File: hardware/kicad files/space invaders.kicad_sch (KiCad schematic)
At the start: 43 parts, among them J1 ICSP, J10 DE9_Socket, J2 RE, J3 RD, J4 RC5/6/7, J5 RC0/1/2, J6 RA6/7, J7 Conn_01x04_Pin, J8 RB1/2/3/4/5, J9 USB_C_Receptacle_PowerOnly_6P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

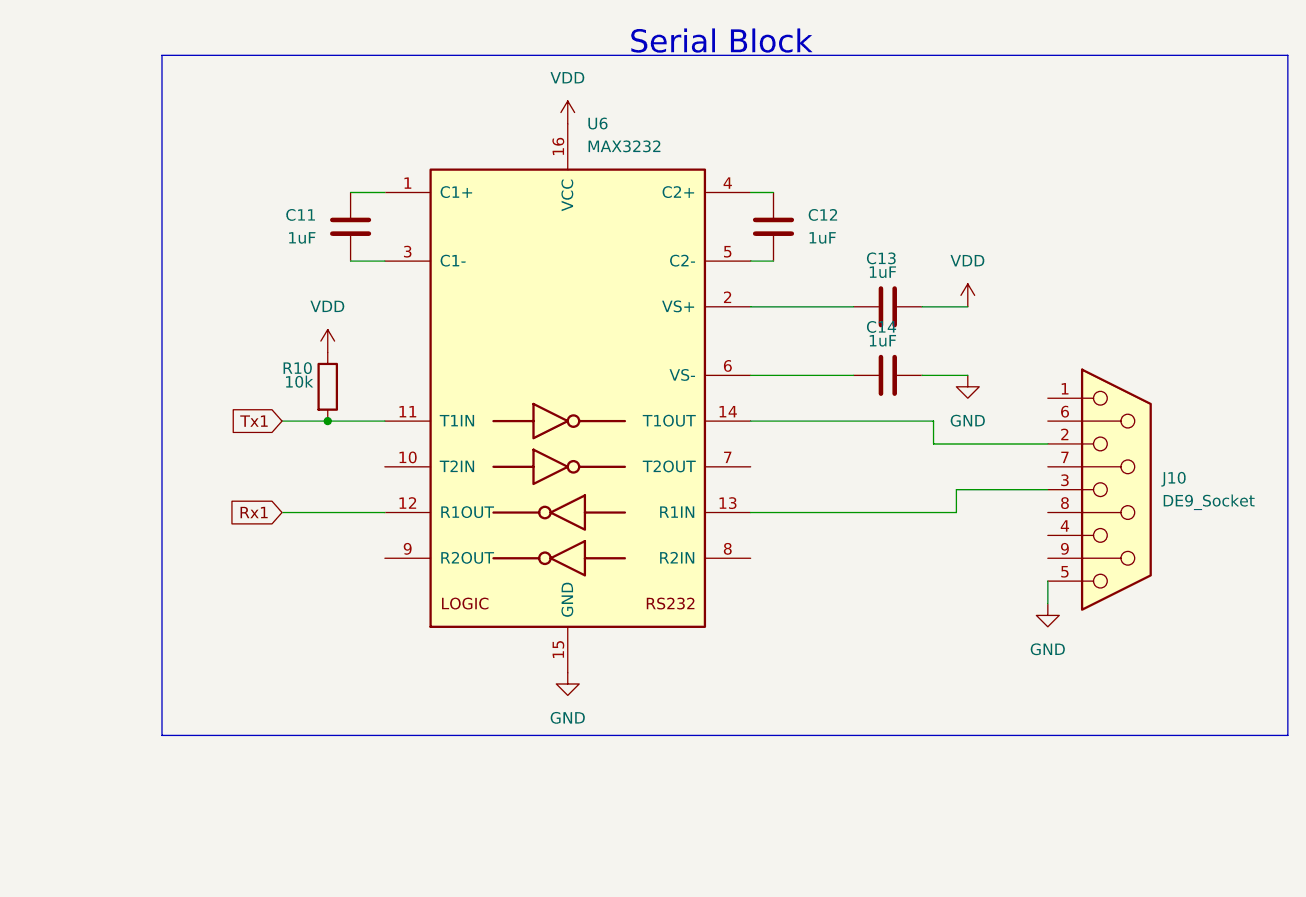
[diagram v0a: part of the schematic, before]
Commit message: Added Serial to PCB
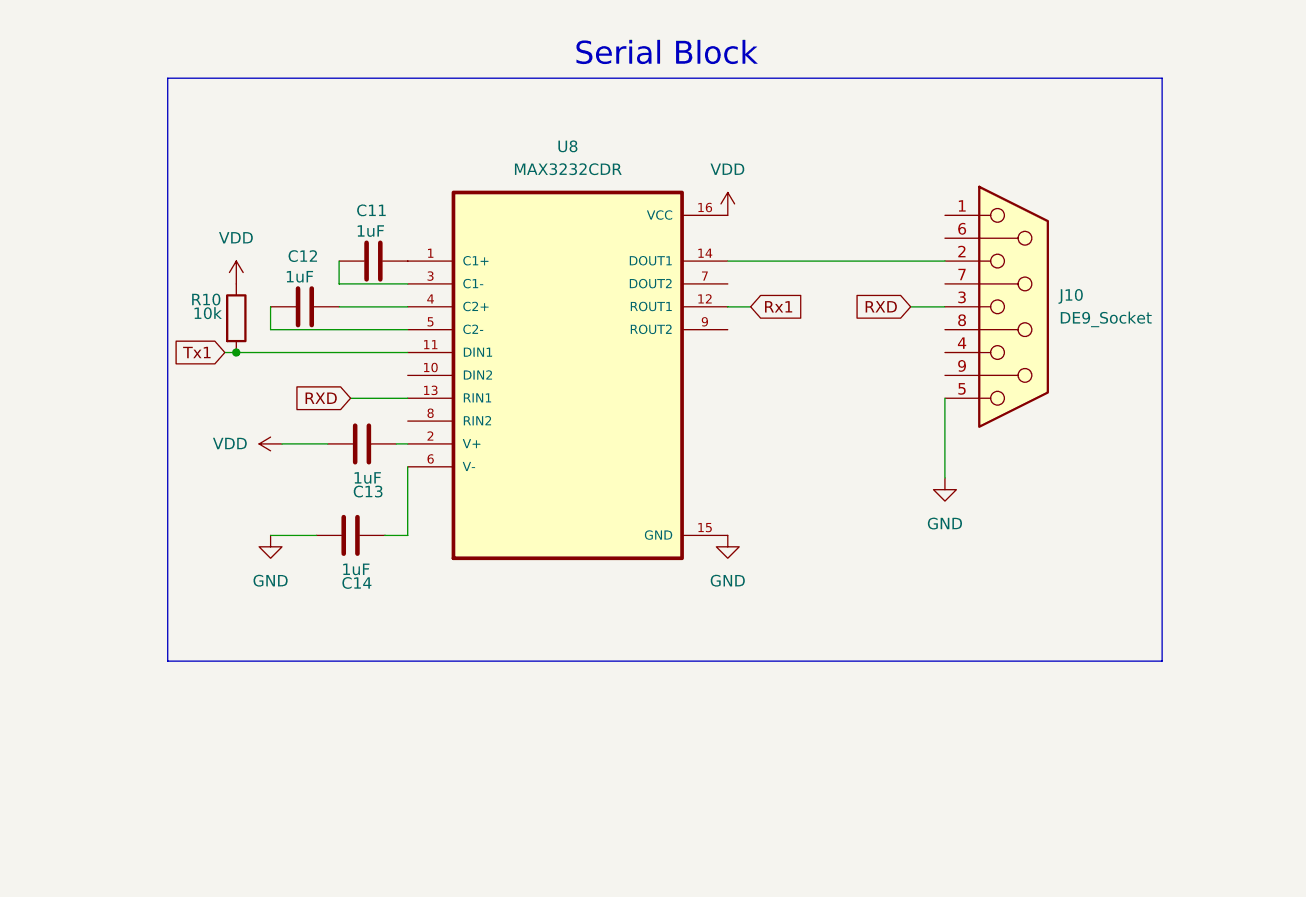
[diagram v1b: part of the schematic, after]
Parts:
- removed U6: MAX3232, symbol Interface_UART:MAX3232
- added U8: MAX3232CDR, Package_SO:SOIC-16_3.9x9.9mm_P1.27mm, symbol MAX3232CDR:MAX3232CDR
- J10: footprint (none) -> Connector_Dsub:DSUB-9_Pins_Horizontal_P2.77x2.84mm_EdgePinOffset7.70mm_Housed_MountingHolesOffset9.12mm
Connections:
- net GND: now also U8.15 (GND)
- net Rx1: now also U8.12 (ROUT1)
- net Tx1: now also U8.11 (DIN1)
- net VDD: now also U8.16 (VCC)
- net at C14.2: now also U8.6 (V-)
- net at C13.2: now also U8.2 (V+)
- net at J10.2: now also U8.14 (DOUT1)
- net RXD: now reaches J10.3
- net RXD: now also U8.13 (RIN1)
- net at C11.1: now also U8.1 (C1+)
- net at C11.2: now also U8.3 (C1-)
- net at C12.1: now also U8.4 (C2+)
- net at C12.2: now also U8.5 (C2-)
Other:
- moved on the sheet: C11, C12, C13, C14, J10, R10
